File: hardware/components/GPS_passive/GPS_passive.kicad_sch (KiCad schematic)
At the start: 18 parts, among them U101 NEO-M9N

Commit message: LCSC部品番号割り当て
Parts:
- C101: LCSC (none) -> C1525
- C102: LCSC (none) -> C52923
- R101, R102: LCSC (none) -> C25768
- R103, R104: LCSC (none) -> C25105
- R105: LCSC (none) -> C25530
- R106: LCSC (none) -> C11702
- R107: LCSC (none) -> C25139
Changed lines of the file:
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@@
 			)
 		)
-		(property "LCSC" ""
+		(property "LCSC" "C1525"
 			(at 215.265 127 0)
 			(effects
@@
 			)
 		)
-		(property "LCSC" ""
+		(property "LCSC" "C25530"
 			(at 140.97 110.49 0)
 			(effects
@@
 			)
 		)
-		(property "LCSC" ""
+		(property "LCSC" "C25105"
 			(at 134.62 77.47 0)
 			(effects
@@
 			)
 		)
-		(property "LCSC" ""
+		(property "LCSC" "C25768"
 			(at 92.075 74.93 0)
 			(effects
@@
 			)
 		)
-		(property "LCSC" ""
+		(property "LCSC" "C11702"
 			(at 207.01 67.31 0)
 			(effects
@@
 			)
 		)
-		(property "LCSC" ""
+		(property "LCSC" "C52923"
 			(at 223.52 81.28 0)
 			(effects
@@
 			)
 		)
-		(property "LCSC" ""
+		(property "LCSC" "C25105"
 			(at 134.62 80.01 0)
 			(effects
@@
 			)
 		)
-		(property "LCSC" ""
+		(property "LCSC" "C25768"
 			(at 92.075 72.39 0)
 			(effects
@@
 			)
 		)
-		(property "LCSC" ""
+		(property "LCSC" "C25139"
 			(at 208.28 121.92 0)
 			(effects

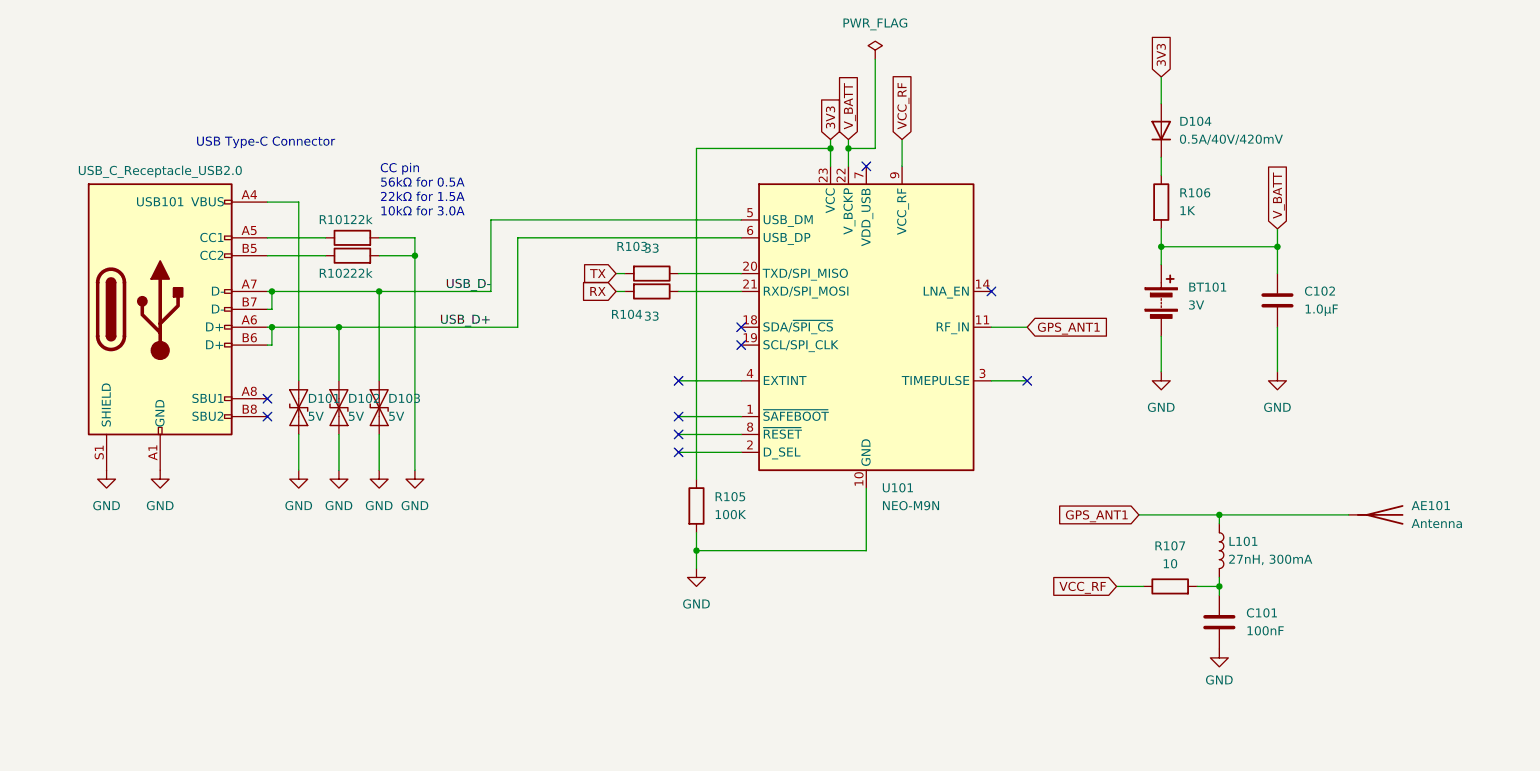
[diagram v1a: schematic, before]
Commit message: SMAコネクタ等ちょいちょい変更しました
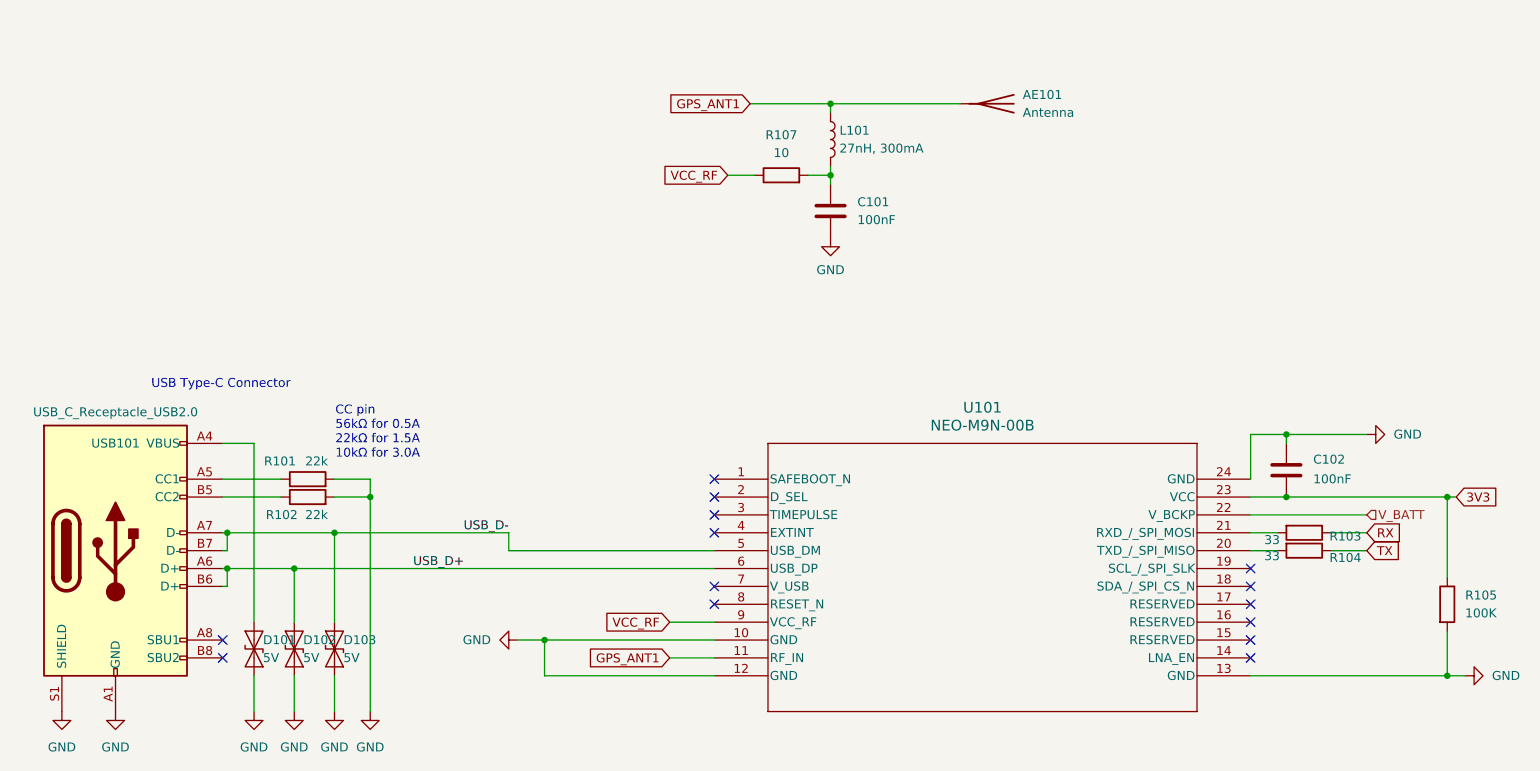
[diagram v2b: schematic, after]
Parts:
- removed BT101: 3V, Battery:Battery_Panasonic_CR2032-HFN_Horizontal_CircularHoles, symbol Device:Battery
- removed D104: 0.5A/40V/420mV, Diode_SMD:D_0402_1005Metric, symbol Device:D
- removed R106: 1K, Resistor_SMD:R_0402_1005Metric, symbol Device:R
- removed U101: NEO-M9N, RF_GPS:ublox_NEO, symbol RF_GPS:NEO-M9N
- added U101: NEO-M9N-00B, WOBClibrary:SMT_9N-00B_UBL, symbol WOBClibrary:NEO-M9N-00B
- AE101: footprint WOBCLibrary:GNSS_Antenna_1212 -> WOBClibrary:GNSS_Antenna_1212
- C102: value 1.0μF -> 100nF; LCSC C52923 -> C1525
- D101, D102, D103: footprint Diode_SMD:D_SOD-923 -> Diode_SMD:D_SOD-882D; LCSC (none) -> C7420372
- USB101: LCSC (none) -> C2982481
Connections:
- net 3V3: now also C102.2, U101.23 (VCC)
- net GND: now also C102.1, U101.10 (GND), U101.12 (GND), U101.13 (GND), U101.24 (GND); no longer C102.2
- net GPS_ANT1: now also U101.11 (RF_IN)
- net RX: now also R103.1; no longer R104.2
- net TX: now also R104.1; no longer R103.2
- net USB_D+: now also U101.6 (USB_DP)
- net USB_D-: now also U101.5 (USB_DM)
- net VCC_RF: now also U101.9 (VCC_RF)
- net V_BATT: now also U101.22 (V_BCKP); no longer C102.1
- new net: R104.2, U101.20 (TXD_/_SPI_MISO)
- new net: R103.2, U101.21 (RXD_/_SPI_MOSI)
- no-connect marks 11 -> 14
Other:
- moved on the sheet: AE101, C101, L101, R107

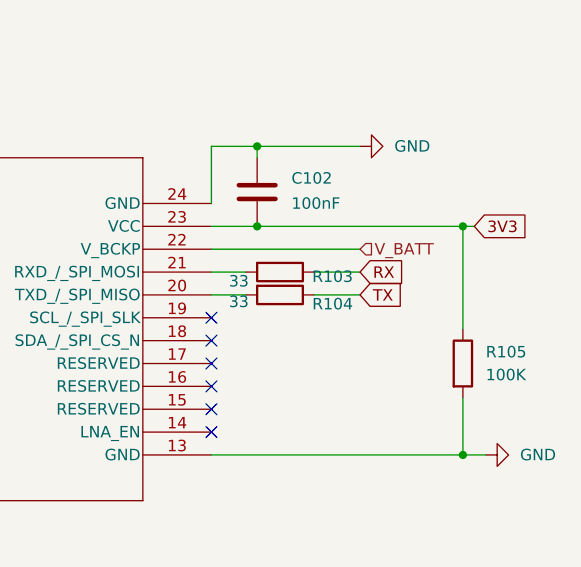
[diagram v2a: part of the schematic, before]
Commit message: Trackerモジュールを作り始めました。あと、GPSのTX,RXを階層ラベルに変更しました。
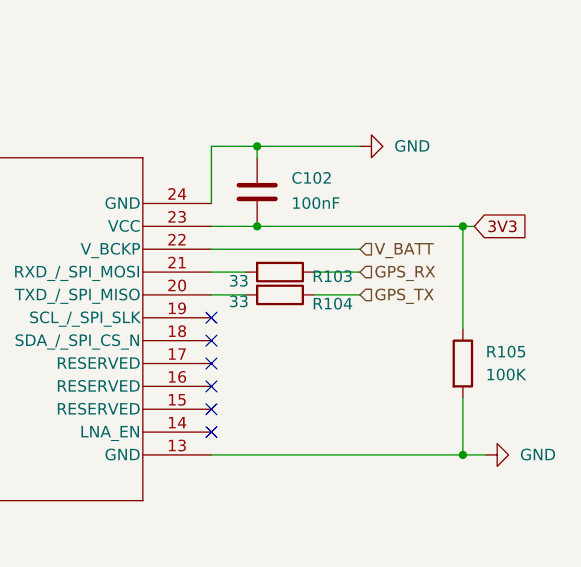
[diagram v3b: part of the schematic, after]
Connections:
- net RX renamed GPS_RX
- net TX renamed GPS_TX
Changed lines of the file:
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@@
-		)
-	)
-	(global_label "TX"
-		(shape input)
-		(at 236.22 116.84 0)
-		(fields_autoplaced yes)
-		(effects
-			(font
-				(size 1.27 1.27)
-			)
-			(justify left)
-		)
-		(property "Intersheetrefs" "${INTERSHEET_REFS}"
-			(at 241.3823 116.84 0)
-			(effects
-				(font
-					(size 1.27 1.27)
-				)
-				(justify left)
-				(hide yes)
-			)
 		)
 	)
@@
 		)
 	)
-	(global_label "RX"
+	(hierarchical_label "GPS_TX"
 		(shape input)
-		(at 236.22 114.3 0)
+		(at 236.22 116.84 0)
 		(fields_autoplaced yes)
 		(effects
@@
 			(justify left)
 		)
-		(property "Intersheetrefs" "${INTERSHEET_REFS}"
-			(at 241.6847 114.3 0)
-			(effects
-				(font
-					(size 1.27 1.27)
-				)
-				(justify left)
-				(hide yes)
-			)
-		)
 	)
 	(hierarchical_label "V_BATT"
@@
 		(fields_autoplaced yes)
 		(effects
+			(font
+				(size 1.27 1.27)
+			)
+			(justify left)
+		)
+	)
+	(hierarchical_label "GPS_RX"
+		(shape input)
+		(at 236.22 114.3 0)
+		(fields_autoplaced yes)
+		(effects
